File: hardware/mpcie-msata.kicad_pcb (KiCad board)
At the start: 4 copper layers, 100 x 85 mm, 153 parts, among them J101 USB-A, J102 TNG-Power-BTM, J103 TNG-Power-TOP, J104 TNG-Data-BTM, J105 TNG-Data-TOP, P101 Debug, P102 PE, P202 PWR IN, SW101 BOOT, T201 744272251, U101 USB2517, U102 MIC2026-1YM, U103 82400152, U104 STM32F070CBT6, U105 TPD4S010DQA, U106 TPD4S010DQA, U107 TPD4S010DQA, U110 TPS22975, U112 VN7140AS, U201 AZ1117EH, U203 BD90640HFP, U204 PAC1933, X101 24MHz, X102 TBD

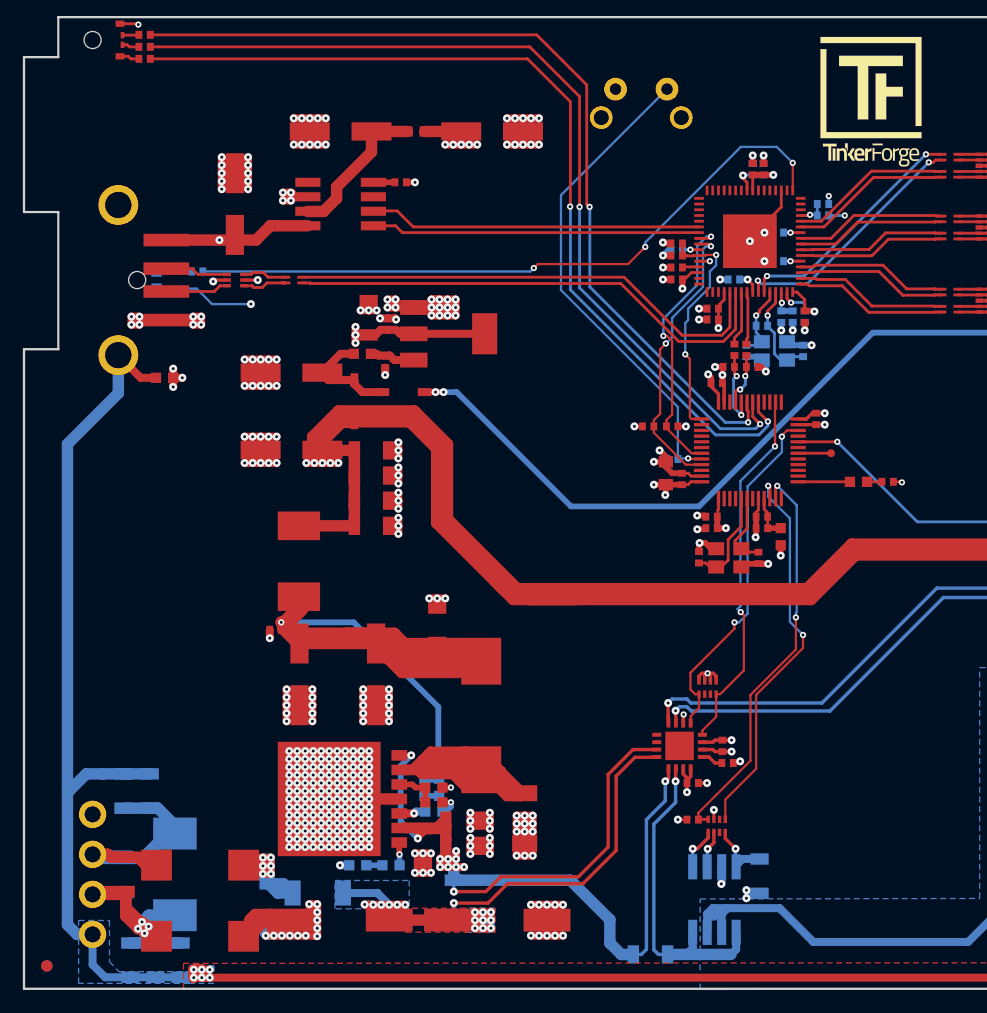
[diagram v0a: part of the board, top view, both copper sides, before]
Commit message: schematic improved
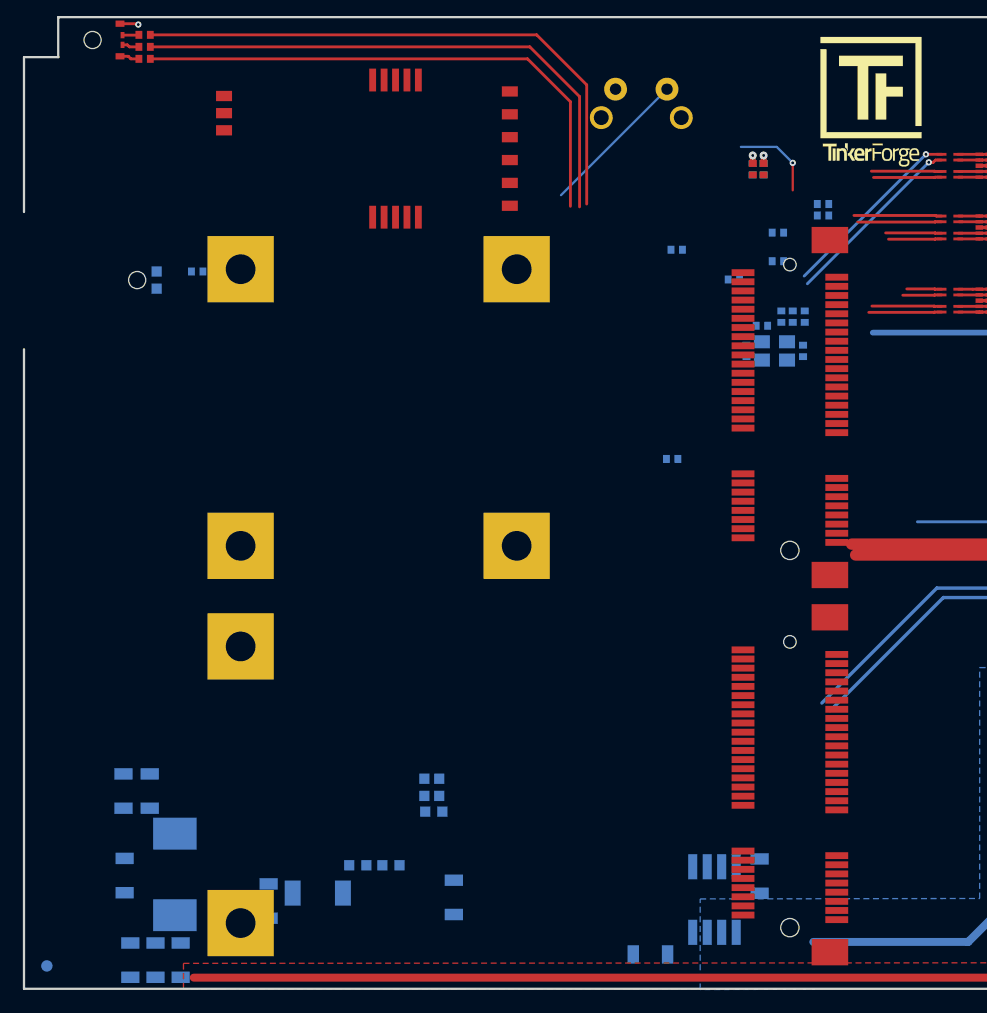
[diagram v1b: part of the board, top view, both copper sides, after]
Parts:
- removed C107, C110, C112, C116, C127, C129, C130, C131, C133, C214, C221, C222: 100nF, C0402F
- removed C108, C109, C117: >100uF, ELKO_63
- removed C115, C123, C124, C209, C226: 1uF, C0402F
- removed C120: 100nF, C0603F
- removed C121, C122: TBD/47pF, C0402F
- removed C137, C138: TBD, C0402F
- removed C139: 10uF, C0805
- removed C201, C202, C215, C218, C223, C224, C225, C227: 10uF, C1206
- removed C203: TBD, kicad-libraries:ELKO_63
- removed C205: 100nF, C1206
- removed C208: 100pF, C0603F
- removed C212, C213: UWT1H221MNL1GS, kicad-libraries:ELKO_103
- removed C216, C219, C220: >100µF, kicad-libraries:ELKO_63
- removed D102: LED, D0603F
- removed D202, D203: B0520LW-7-F, kicad-libraries:SOD-123
- removed D206: PMEG6045, SOD-128
- removed the Fiducial_Mark at (59.5, 133.9)
- removed J101: USB-A, kicad-libraries:USB-A-SMT-8231
- removed L101, L201: INDUCTs, R0603F
- removed L102: 744230900, WE-CNSW-0603
- removed L108: FB, R0603F
- removed L202: 22uH 74437368220, WE-LHMI
- removed L203: 10uH, SRP7030
- removed P101: Debug, kicad-libraries:DEBUG_PAD
- removed P202: PWR IN, OQ_4P
- removed R101, R105, R106, R111, R117, R218: 10k, R0402F
- removed R102: 100k, R0402F
- removed R112, R113: 22, R0402F
- removed R121: 1k, R0402F
- removed R204: VC1206K201R030, R1206
- removed R208: 27, R0603F
- removed RP102, RP201: 10k, kicad-libraries:4X0402
- removed T201: 744272251, kicad-libraries:WE-SL5
- removed U101: USB2517, kicad-libraries:QFN64-9x9mm-0.5mm_USB2517
- removed U102: MIC2026-1YM, kicad-libraries:SO-8
- removed U103: 82400152, SOT563-SPEC
- removed U104: STM32F070CBT6, kicad-libraries:LQFP48
- removed U201: AZ1117EH, kicad-libraries:SOT-223
- removed U203: BD90640HFP, BD906XX-C-HRP7
- removed U204: PAC1933, kicad-libraries:QFN-16
- removed X102: TBD, kicad-libraries:CRYSTAL_3225
- added REF**: Mini-SATA, kicad-libraries:Mini-SATA, F.Cu at (124.5, 122.0)
- added REF**: Mini-PCIE, kicad-libraries:Mini-PCIE, F.Cu at (124.5, 89.0)
- added REF**: LM813, kicad-libraries:LM813, F.Cu at (87.5, 62.5)
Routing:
- net GND: track 859.2 -> 125.7 mm, vias 402 -> 49
- net +5V: track 270.4 -> 115.9 mm, vias 10 -> 0
- net CUR1-: track 104.3 -> 0.00 mm, vias 12 -> 0
- net Net-(C214-Pad1): track 88.7 -> 0.00 mm, vias 1 -> 0
- net Earth: track 251.7 -> 170.1 mm, vias 31 -> 25
- net 3V3: track 78.9 -> 2.33 mm, vias 32 -> 2
- net Net-(R104-Pad1): track 59.3 -> 0.00 mm, vias 3 -> 0
- net Net-(D206-Pad2): track 58.3 -> 0.00 mm
- net CUR1+: track 70.1 -> 12.8 mm, vias 16 -> 0
- net 5V_STACK_UP: track 111.9 -> 60.0 mm, vias 2 -> 0
- net EXT_USB_D+: track 43.8 -> 0.00 mm
- net EXT_USB_D-: track 42.9 -> 0.00 mm
- net Net-(C204-Pad2): track 41.6 -> 0.00 mm, vias 4 -> 0
- net SW_24_STACK: track 35.5 -> 0.00 mm, vias 2 -> 0
- net SW_24_CUR: track 34.5 -> 0.00 mm, vias 2 -> 0
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- removed copper zone on B.Cu, net CUR1+
- removed copper zone on F.Cu, net CUR1+
- removed copper zone on B.Cu, net Earth
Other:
- outline, holes or cut-outs redrawn
- board text removed: "FE"
- board text removed: "GND"
- board text removed: "NC"
- board text removed: "VCC"

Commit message: schematic nearly finished
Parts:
- added REF**: QFP-64_7x7_Pitch0.4mm, kicad-libraries:QFP-64_7x7_Pitch0.4mm, F.Cu at (94.3, 112.2)
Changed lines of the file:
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@@
     (tracks 533)
     (zones 0)
-    (modules 77)
+    (modules 78)
     (nets 66)
   )
@@
     (add_net STACK_USB_D4_F-)
   )
+  (module kicad-libraries:QFP-64_7x7_Pitch0.4mm (layer F.Cu)
+    (at 94.35 112.15)
+    (attr smd)
+    (fp_text reference REF** (at 0 -0.6) (layer F.Fab)
+      (effects (font (size 0.15 0.15) (thickness 0.0375)))
+    )
+    (fp_text value QFP-64_7x7_Pitch0.4mm (at 0 0.6) (layer F.Fab)
+      (effects (font (size 0.15 0.15) (thickness 0.0375)))
+    )
+    (fp_line (start 3.5 -3.5) (end -2.5 -3.5) (layer F.Fab) (width 0.1))
+    (fp_line (start 3.5 3.5) (end 3.5 -3.5) (layer F.Fab) (width 0.1))
+    (fp_line (start -3.5 3.5) (end 3.5 3.5) (layer F.Fab) (width 0.1))
+    (fp_line (start -3.5 -2.5) (end -3.5 3.5) (layer F.Fab) (width 0.1))
+    (fp_line (start -2.5 -3.5) (end -3.5 -2.5) (layer F.Fab) (width 0.1))
+    (pad EP smd rect (at 0 0) (size 4 4) (layers F.Cu F.Paste F.Mask))
+    (pad 64 smd oval (at -3 -4) (size 0.19 1.2) (layers F.Cu F.Paste F.Mask))
+    (pad 63 smd oval (at -2.6 -4) (size 0.19 1.2) (layers F.Cu F.Paste F.Mask))
+    (pad 62 smd oval (at -2.2 -4) (size 0.19 1.2) (layers F.Cu F.Paste F.Mask))
+    (pad 61 smd oval (at -1.8 -4) (size 0.19 1.2) (layers F.Cu F.Paste F.Mask))
+    (pad 60 smd oval (at -1.4 -4) (size 0.19 1.2) (layers F.Cu F.Paste F.Mask))
+    (pad 59 smd oval (at -1 -4) (size 0.19 1.2) (layers F.Cu F.Paste F.Mask))
+    (pad 58 smd oval (at -0.6 -4) (size 0.19 1.2) (layers F.Cu F.Paste F.Mask))
+    (pad 57 smd oval (at -0.2 -4) (size 0.19 1.2) (layers F.Cu F.Paste F.Mask))
+    (pad 56 smd oval (at 0.2 -4) (size 0.19 1.2) (layers F.Cu F.Paste F.Mask))
+    (pad 55 smd oval (at 0.6 -4) (size 0.19 1.2) (layers F.Cu F.Paste F.Mask))
+    (pad 54 smd oval (at 1 -4) (size 0.19 1.2) (layers F.Cu F.Paste F.Mask))
+    (pad 53 smd oval (at 1.4 -4) (size 0.19 1.2) (layers F.Cu F.Paste F.Mask))
+    (pad 52 smd oval (at 1.8 -4) (size 0.19 1.2) (layers F.Cu F.Paste F.Mask))
+    (pad 51 smd oval (at 2.2 -4) (size 0.19 1.2) (layers F.Cu F.Paste F.Mask))
+    (pad 50 smd oval (at 2.6 -4) (size 0.19 1.2) (layers F.Cu F.Paste F.Mask))
+    (pad 49 smd oval (at 3 -4) (size 0.19 1.2) (layers F.Cu F.Paste F.Mask))
+    (pad 48 smd oval (at 4 -3 90) (size 0.19 1.2) (layers F.Cu F.Paste F.Mask))
+    (pad 47 smd oval (at 4 -2.6 90) (size 0.19 1.2) (layers F.Cu F.Paste F.Mask))
+    (pad 46 smd oval (at 4 -2.2 90) (size 0.19 1.2) (layers F.Cu F.Paste F.Mask))
+    (pad 45 smd oval (at 4 -1.8 90) (size 0.19 1.2) (layers F.Cu F.Paste F.Mask))
+    (pad 44 smd oval (at 4 -1.4 90) (size 0.19 1.2) (layers F.Cu F.Paste F.Mask))
+    (pad 43 smd oval (at 4 -1 90) (size 0.19 1.2) (layers F.Cu F.Paste F.Mask))
+    (pad 42 smd oval (at 4 -0.6 90) (size 0.19 1.2) (layers F.Cu F.Paste F.Mask))
+    (pad 41 smd oval (at 4 -0.2 90) (size 0.19 1.2) (layers F.Cu F.Paste F.Mask))
+    (pad 40 smd oval (at 4 0.2 90) (size 0.19 1.2) (layers F.Cu F.Paste F.Mask))
+    (pad 39 smd oval (at 4 0.6 90) (size 0.19 1.2) (layers F.Cu F.Paste F.Mask))
+    (pad 38 smd oval (at 4 1 90) (size 0.19 1.2) (layers F.Cu F.Paste F.Mask))
+    (pad 37 smd oval (at 4 1.4 90) (size 0.19 1.2) (layers F.Cu F.Paste F.Mask))
+    (pad 36 smd oval (at 4 1.8 90) (size 0.19 1.2) (layers F.Cu F.Paste F.Mask))
+    (pad 35 smd oval (at 4 2.2 90) (size 0.19 1.2) (layers F.Cu F.Paste F.Mask))
+    (pad 34 smd oval (at 4 2.6 90) (size 0.19 1.2) (layers F.Cu F.Paste F.Mask))
+    (pad 33 smd oval (at 4 3 90) (size 0.19 1.2) (layers F.Cu F.Paste F.Mask))
+    (pad 32 smd oval (at 3 4) (size 0.19 1.2) (layers F.Cu F.Paste F.Mask))
+    (pad 31 smd oval (at 2.6 4) (size 0.19 1.2) (layers F.Cu F.Paste F.Mask))
+    (pad 30 smd oval (at 2.2 4) (size 0.19 1.2) (layers F.Cu F.Paste F.Mask))
+    (pad 29 smd oval (at 1.8 4) (size 0.19 1.2) (layers F.Cu F.Paste F.Mask))
+    (pad 28 smd oval (at 1.4 4) (size 0.19 1.2) (layers F.Cu F.Paste F.Mask))
+    (pad 27 smd oval (at 1 4) (size 0.19 1.2) (layers F.Cu F.Paste F.Mask))
+    (pad 26 smd oval (at 0.6 4) (size 0.19 1.2) (layers F.Cu F.Paste F.Mask))
+    (pad 25 smd oval (at 0.2 4) (size 0.19 1.2) (layers F.Cu F.Paste F.Mask))
+    (pad 24 smd oval (at -0.2 4) (size 0.19 1.2) (layers F.Cu F.Paste F.Mask))
+    (pad 23 smd oval (at -0.6 4) (size 0.19 1.2) (layers F.Cu F.Paste F.Mask))
+    (pad 22 smd oval (at -1 4) (size 0.19 1.2) (layers F.Cu F.Paste F.Mask))
+    (pad 21 smd oval (at -1.4 4) (size 0.19 1.2) (layers F.Cu F.Paste F.Mask))
+    (pad 20 smd oval (at -1.8 4) (size 0.19 1.2) (layers F.Cu F.Paste F.Mask))
+    (pad 19 smd oval (at -2.2 4) (size 0.19 1.2) (layers F.Cu F.Paste F.Mask))
+    (pad 18 smd oval (at -2.6 4) (size 0.19 1.2) (layers F.Cu F.Paste F.Mask))
+    (pad 17 smd oval (at -3 4) (size 0.19 1.2) (layers F.Cu F.Paste F.Mask))
+    (pad 16 smd oval (at -4 3 90) (size 0.19 1.2) (layers F.Cu F.Paste F.Mask))
+    (pad 15 smd oval (at -4 2.6 90) (size 0.19 1.2) (layers F.Cu F.Paste F.Mask))
+    (pad 14 smd oval (at -4 2.2 90) (size 0.19 1.2) (layers F.Cu F.Paste F.Mask))
+    (pad 13 smd oval (at -4 1.8 90) (size 0.19 1.2) (layers F.Cu F.Paste F.Mask))
+    (pad 12 smd oval (at -4 1.4 90) (size 0.19 1.2) (layers F.Cu F.Paste F.Mask))
+    (pad 11 smd oval (at -4 1 90) (size 0.19 1.2) (layers F.Cu F.Paste F.Mask))
+    (pad 10 smd oval (at -4 0.6 90) (size 0.19 1.2) (layers F.Cu F.Paste F.Mask))
+    (pad 9 smd oval (at -4 0.2 90) (size 0.19 1.2) (layers F.Cu F.Paste F.Mask))
+    (pad 8 smd oval (at -4 -0.2 90) (size 0.19 1.2) (layers F.Cu F.Paste F.Mask))
+    (pad 7 smd oval (at -4 -0.6 90) (size 0.19 1.2) (layers F.Cu F.Paste F.Mask))
+    (pad 6 smd oval (at -4 -1 90) (size 0.19 1.2) (layers F.Cu F.Paste F.Mask))
+    (pad 5 smd oval (at -4 -1.4 90) (size 0.19 1.2) (layers F.Cu F.Paste F.Mask))
+    (pad 4 smd oval (at -4 -1.8 90) (size 0.19 1.2) (layers F.Cu F.Paste F.Mask))
+    (pad 3 smd oval (at -4 -2.2 90) (size 0.19 1.2) (layers F.Cu F.Paste F.Mask))
+    (pad 2 smd oval (at -4 -2.6 90) (size 0.19 1.2) (layers F.Cu F.Paste F.Mask))
+    (pad 1 smd oval (at -4 -3 90) (size 0.19 1.2) (layers F.Cu F.Paste F.Mask))
+  )
   (module kicad-libraries:Mini-SATA (layer F.Cu)

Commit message: fix schematic first placement
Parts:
- removed C210: 4.7nF, C0603F
- removed C211: 10nF, C1206
- removed C217: DNP, C0603F
- removed D101: LED green, LED-LP
- removed D201: 3.0SMI30CATR, kicad-libraries:SMC
- removed D205: PMEG6045, SOD-128
- removed R209: 1M, R1206
- removed R212: 20k, R0603F
- removed R214: 47k, R0603F
- removed R215: 8.2k, R0603F
- removed R219, R220, R221: 0.02, R1206
- removed REF**: QFP-64_7x7_Pitch0.4mm, kicad-libraries:QFP-64_7x7_Pitch0.4mm
- removed REF**: Mini-SATA, kicad-libraries:Mini-SATA
- removed REF**: Mini-PCIE, kicad-libraries:Mini-PCIE
- removed REF**: LM813, kicad-libraries:LM813
- removed U106, U107: TPD4S010DQA, TPD4S010DQA
- removed U110: TPS22975, WSON8-2x2
- removed U112: VN7140AS, kicad-libraries:SO-8
- added C107: 100nF, C0402F, B.Cu at (133.2, 70.2)
- added C108: 1uF, C0402F, F.Cu at (134.1, 67.2)
- added C109: 1uF, C0402F, F.Cu at (132.2, 64.5)
- added C110: 100nF, C0402F, B.Cu at (128.8, 67.2)
- added C112: 100nF, C0402F, B.Cu at (137.8, 63.5)
- added C115: 1uF, C0402F, F.Cu at (133.2, 70.2)
- added C116: 10uF, C0805, F.Cu at (129.3, 59.2)
- added C117: 100nF, C0402F, B.Cu at (134.6, 60.1)
- added C120: 1uF, C0402F, F.Cu at (137.2, 68.0)
- added C121: TBD/47pF, C0402F, F.Cu at (128.0, 71.3)
- added C122: TBD/47pF, C0402F, F.Cu at (128.0, 69.2)
- added C123: 1uF, C0402F, F.Cu at (223.2, 70.8)
- added C124: 1uF, C0402F, F.Cu at (237.8, 87.3)
- added C127: 100nF, C0402F, F.Cu at (230.7, 95.3)
- added C129: 100nF, C0402F, F.Cu at (217.2, 74.2)
- added C130: 100nF, C0402F, F.Cu at (232.1, 87.7)
- added C131: 100nF, C0402F, F.Cu at (224.2, 79.0)
- added C133: 100nF, C0402F, F.Cu at (233.5, 93.4)
- added C137: TBD, C0402F, F.Cu at (222.2, 93.5)
- added C138: TBD, C0402F, F.Cu at (219.3, 70.5)
- added C139: 10uF, C0805, F.Cu at (201.1, 96.1)
- added C140: 10uF, C0805, F.Cu at (139.4, 94.0)
- added C141: 1uF, C0402F, F.Cu at (126.5, 57.8)
- added C142: 1uF, C0402F, F.Cu at (140.8, 94.5)
- added C143: 1uF, C0402F, F.Cu at (146.9, 92.7)
- added C144: 1uF, C0402F, F.Cu at (134.4, 53.4)
- added C145: >100uF, ELKO_63, F.Cu at (103.0, 61.8)
- added C146: 10uF, C0805, F.Cu at (146.7, 91.3)
- added C147: 10uF, C0805, F.Cu at (135.8, 53.9)
- added C148: >100uF, ELKO_63, F.Cu at (144.8, 87.2)
- added C150: >100uF, ELKO_63, F.Cu at (139.9, 57.2)
- added C151: >100uF, ELKO_63, F.Cu at (153.7, 87.2)
- added C201: 10uF, C0805, B.Cu at (115.0, 128.1)
- added C202: >100uF, ELKO_63, F.Cu at (129.4, 107.5)
- added C203: 10uF, C0805, B.Cu at (115.0, 116.0)
- added C205: 10uF, C0805, B.Cu at (124.0, 108.5)
- added C208: 10uF, C0805, B.Cu at (100.8, 60.0)
- added C209: 10uF, C0805, F.Cu at (135.8, 102.2)
- added C301: 10uF, C0805, B.Cu at (115.0, 95.0)
- added C302: 10uF, C0805, B.Cu at (115.0, 83.2)
- added C303: 10uF, C0805, B.Cu at (124.0, 78.8)
- added C304: 10uF, C0805, B.Cu at (124.0, 75.5)
- added C305: 10uF, C0805, B.Cu at (115.0, 72.7)
- added C306: >100uF, ELKO_63, F.Cu at (129.6, 93.8)
- added C308: 100nF, kicad-libraries:C0402E, F.Cu at (359.6, 80.7)
- added C309: 10uF, C0805, F.Cu at (135.8, 93.8)
- added C310: 10nF, kicad-libraries:C0402E, F.Cu at (126.2, 79.8)
- added C311: 10nF, kicad-libraries:C0402E, F.Cu at (126.2, 81.0)
- added C312: 10nF, kicad-libraries:C0402E, F.Cu at (126.2, 83.0)
- added C313: 10nF, kicad-libraries:C0402E, F.Cu at (126.2, 84.2)
- added C314: 100nF, kicad-libraries:C0402E, F.Cu at (343.2, 95.2)
- added C315: 100nF, kicad-libraries:C0402E, F.Cu at (346.3, 92.4)
- added C316: 100nF, kicad-libraries:C0402E, F.Cu at (334.6, 104.0)
- added C317: 100nF, kicad-libraries:C0402E, F.Cu at (338.9, 97.6)
- added C318: 100nF, kicad-libraries:C0402E, F.Cu at (356.6, 80.7)
- added C319: 100nF, kicad-libraries:C0402E, F.Cu at (334.6, 100.2)
- added C320: 100nF, kicad-libraries:C0402E, F.Cu at (347.6, 89.6)
- added C321: 100nF, kicad-libraries:C0402E, F.Cu at (334.6, 102.1)
- added C322: 100nF, kicad-libraries:C0402E, F.Cu at (350.6, 89.6)
- added C323: 100nF, kicad-libraries:C0402E, F.Cu at (356.6, 82.6)
- added C324: 100nF, kicad-libraries:C0402E, F.Cu at (349.3, 91.5)
- added C325: 10uF, C0805, F.Cu at (348.2, 84.7)
- added C326: 10uF, C0805, F.Cu at (335.3, 98.0)
- added C327: 10uF, C0805, F.Cu at (353.0, 81.0)
- added C328: 10uF, C0805, F.Cu at (343.9, 90.2)
- added C329: 10uF, C0805, F.Cu at (366.6, 68.3)
- added C330: 10uF, C0805, F.Cu at (343.9, 87.6)
- added C331: 10uF, C0805, F.Cu at (353.0, 78.4)
- added C332: 100nF, kicad-libraries:C0402E, F.Cu at (354.9, 86.4)
- added C333: 100nF, kicad-libraries:C0402E, F.Cu at (337.6, 102.1)
- added C334: 100nF, kicad-libraries:C0402E, F.Cu at (337.6, 104.0)
- added C335: 100nF, kicad-libraries:C0402E, F.Cu at (340.6, 99.5)
- added C336: 100nF, kicad-libraries:C0402E, F.Cu at (346.3, 94.3)
- added C337: 100nF, kicad-libraries:C0402E, F.Cu at (354.9, 84.5)
- added C338: 100nF, kicad-libraries:C0402E, F.Cu at (373.2, 67.9)
- added C339: 10uF, C0805, F.Cu at (335.3, 90.2)
- added C340: 10uF, C0805, F.Cu at (339.6, 87.6)
- added C341: 10uF, C0805, F.Cu at (335.3, 87.6)
- added C342: 10uF, C0805, F.Cu at (339.6, 85.0)
- added C343: 100nF, kicad-libraries:C0402E, F.Cu at (351.9, 87.2)
- added C344: 100nF, kicad-libraries:C0402E, F.Cu at (370.2, 69.8)
- added C345: 10uF, C0805, F.Cu at (339.9, 79.8)
- added C346: 10uF, C0805, F.Cu at (335.3, 95.4)
- added C347: 100nF, kicad-libraries:C0402E, F.Cu at (337.6, 100.2)
- added D102: LED, D0603F, F.Cu at (117.2, 57.6)
- added J201: Mini-PCIE, kicad-libraries:Mini-PCIE, F.Cu at (119.5, 121.0)
- added J202: SIM8060, kicad-libraries:SIM8060, F.Cu at (133.2, 115.0)
- added J301: Mini-SATA, kicad-libraries:Mini-SATA, F.Cu at (119.5, 88.0)
- added L101: FB, R0603F, F.Cu at (131.2, 60.6)
- added L102: 744230900, WE-CNSW-0603, B.Cu at (128.3, 74.5)
- added L108: FB, R0603F, F.Cu at (225.0, 86.6)
- added L111: INDUCTs, kicad-libraries:R0805E, B.Cu at (150.2, 85.3)
- added L112: INDUCTs, kicad-libraries:R0805E, F.Cu at (146.7, 54.5)
- added L201: INDUCTs, kicad-libraries:R0805E, F.Cu at (134.8, 104.8)
- added L301: INDUCTs, kicad-libraries:R0805E, F.Cu at (134.8, 96.5)
- added L302: INDUCTs, kicad-libraries:R0805E, F.Cu at (353.0, 75.8)
- added L303: INDUCTs, kicad-libraries:R0805E, F.Cu at (339.6, 90.2)
- added L304: INDUCTs, kicad-libraries:R0805E, F.Cu at (335.3, 92.8)
- added L305: INDUCTs, kicad-libraries:R0805E, F.Cu at (343.9, 85.0)
- added P101: Debug, kicad-libraries:DEBUG_PAD, F.Cu at (218.2, 65.2)
- added Q301: 40MHz, kicad-libraries:CRYSTAL_3225, F.Cu at (335.4, 80.3)
- added R101: 10k, R0402F, B.Cu at (137.8, 62.5)
- added R102: 10k, R0402F, F.Cu at (128.2, 65.8)
- added R105: 10k, R0402F, B.Cu at (129.3, 61.2)
- added R106: 10k, R0402F, F.Cu at (235.0, 89.6)
- added R111: DNP, R0402F, F.Cu at (232.1, 91.5)
- added R112: 22, R0402F, B.Cu at (128.3, 69.8)
- added R113: 22, R0402F, B.Cu at (128.3, 70.8)
- added R117: 10k, R0402F, F.Cu at (211.6, 82.8)
- added R121: 1k, R0402F, F.Cu at (117.2, 55.1)
- added R122: 100k, R0402F, B.Cu at (136.2, 58.8)
- added R123: 169k, R0402F, B.Cu at (140.2, 96.3)
- added R124: 30.1k, R0402F, B.Cu at (142.2, 96.3)
- added R201: 1k, kicad-libraries:R0402F, B.Cu at (120.8, 118.5)
- added R202: 1k, kicad-libraries:R0402F, F.Cu at (112.2, 118.2)
- added R203: 1k, kicad-libraries:R0402F, F.Cu at (112.2, 117.2)
- added R204: DNP, kicad-libraries:R0402F, B.Cu at (133.8, 116.8)
- added R205: 1k, kicad-libraries:R0402F, B.Cu at (90.5, 58.8)
- added R301: 0, kicad-libraries:R0402F, F.Cu at (334.6, 107.8)
- added R302: DNP, kicad-libraries:R0402F, F.Cu at (373.2, 69.8)
- added R303: DNP, kicad-libraries:R0402F, F.Cu at (346.2, 96.2)
- added R304: DNP, kicad-libraries:R0402F, F.Cu at (343.6, 99.0)
- added R305: DNP, kicad-libraries:R0402F, F.Cu at (337.6, 105.9)
- added R306: 10k, kicad-libraries:R0402F, F.Cu at (354.8, 88.3)
- added R307: 10k, kicad-libraries:R0402F, F.Cu at (349.3, 93.4)
- added R308: 10k, kicad-libraries:R0402F, F.Cu at (365.0, 78.5)
- added R309: DNP, kicad-libraries:R0402F, F.Cu at (368.9, 74.7)
- added R310: DNP, kicad-libraries:R0402F, F.Cu at (365.0, 76.6)
- added R311: 10k, kicad-libraries:R0402F, F.Cu at (370.0, 71.7)
- added R312: 10k, kicad-libraries:R0402F, F.Cu at (357.9, 84.5)
- added R313: 10k, kicad-libraries:R0402F, F.Cu at (340.6, 101.4)
- added RP201: 1k, kicad-libraries:4X0402, B.Cu at (111.7, 106.5)
- added RP202: 1k, kicad-libraries:4X0402, B.Cu at (101.2, 69.5)
- added RP301: 1k, kicad-libraries:4X0402, F.Cu at (351.9, 84.8)
- added RP302: 100, kicad-libraries:4X0402, F.Cu at (141.6, 82.5)
- added U101: USB2514B, kicad-libraries:QFN36-6x6mm-0.5mm, B.Cu at (133.2, 65.3)
- added U102: LD1117, kicad-libraries:SOT-223, F.Cu at (129.4, 55.1)
- added U103: TPS7A7002, kicad-libraries:SO-8-EP, F.Cu at (145.3, 95.8)
- added U104: STM32F070CBT6, kicad-libraries:LQFP48, B.Cu at (120.0, 65.5)
- added U201: LM813, kicad-libraries:LM813, F.Cu at (86.0, 62.0)
- added U301: TUSB9261PVP, kicad-libraries:QFP-64_7x7_Pitch0.4mm, F.Cu at (134.1, 81.7)
- added U302: TLV71211DBVR, kicad-libraries:SOT23-5, F.Cu at (366.5, 71.6)
- added U303: AP7333-18SAG-7, kicad-libraries:SOT23-3, F.Cu at (361.5, 76.5)
- added U304: AT25DF011-SSHN-T, kicad-libraries:SO-8, B.Cu at (105.7, 81.2)
- added X102: TBD, kicad-libraries:CRYSTAL_3225, F.Cu at (223.9, 61.5)
- C103: value 1uF -> 100nF
- C104, R110, R114: moved to F.Cu
- C105: value 1uF -> 100nF; moved to F.Cu
- C111, C113: value 100nF -> 1uF; moved to F.Cu
- C118: value 100nF -> 1uF
- C125: value 1uF -> 10uF; footprint C0402F -> C0805
- C126: value 1uF -> 1nF; moved to B.Cu
- C128: value 1µF -> 10uF; footprint C0402F -> C0805
- C132: value DNP -> 10uF; footprint C0402F -> C0805
- C135: value 10uF -> 1uF; footprint C1206 -> C0402F
- C136: footprint C1206 -> C0805
- C204: value 10nF -> 10uF; footprint C1206 -> C0805
- C206: value 1nF 2kV -> 10uF; footprint C1206 -> C0805
- C207: value 1nF 2kV -> 10uF; footprint C1206 -> C0805; moved to F.Cu
- L103: value 744230900 -> FB; footprint WE-CNSW-0603 -> R0603F
- L104, R116: moved to B.Cu
- L106, L107, L110: value 744230900 -> INDUCTs; footprint WE-CNSW-0603 -> kicad-libraries:R0805E
- L109: value 742792040 -> 744230900; footprint kicad-libraries:R0805 -> kicad-libraries:WE-CNSW-0603
- R104: value 1k -> 10k; moved to F.Cu
- R107: value 10k -> DNP; moved to F.Cu
- R109: value DNP -> 10k; moved to F.Cu
- R118: value 1k -> DNP; footprint kicad-libraries:1206 -> R0402F
- R206, R207: value VC1206K201R030 -> 1k; footprint R1206 -> kicad-libraries:R0402F
- U105: value TPD4S010DQA -> 82400152; footprint TPD4S010DQA -> SOT563-SPEC
- moved C118 213.5 mm to (327.9, 118.0), turned to 0 degrees
- moved R114 104.5 mm to (212.5, 54.2)
- moved G*** 97.5 mm to (62.9, 127.3)
- moved R207 77.8 mm to (88.5, 58.8), turned to 270 degrees
- moved R118 67.5 mm to (136.7, 60.2), turned to 0 degrees
- moved C207 64.9 mm to (130.7, 113.3), turned to 0 degrees
- moved C204 59.4 mm to (124.0, 111.8), turned to 90 degrees
- moved R104 56.4 mm to (128.2, 63.9)
- moved R206 52.1 mm to (88.5, 70.5), turned to 270 degrees
- moved C206 50.5 mm to (115.0, 105.8)
- moved C128 39.0 mm to (127.8, 61.6), turned to 90 degrees
- moved R116 39.0 mm to (134.6, 59.0)
- moved C136 35.3 mm to (126.0, 59.2), turned to 0 degrees
- moved C126 33.5 mm to (136.7, 61.2), turned to 0 degrees
- moved L109 30.8 mm to (138.4, 64.8), turned to 0 degrees
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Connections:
- C104 pad 1: Net-(C103-Pad1) -> Net-(C104-Pad1)
- C106 pad 1: Net-(C105-Pad1) -> Net-(C103-Pad1)
- C111 pad 1: 3V3 -> Net-(C103-Pad1)
- C113 pad 1: 3V3 -> Net-(C103-Pad1)
- C114 pad 1: 3V3 -> Net-(C107-Pad1)
- C118 pad 1: 3V3 -> Net-(C107-Pad1)
- C119 pad 1: 3V3 -> Net-(C107-Pad1)
- C125 pad 1: GND -> 3V3
- C125 pad 2: +5V -> GND
- C126 pad 1: GND -> Net-(C126-Pad1)
- C126 pad 2: Net-(C126-Pad2) -> GND
- C128 pad 1: Net-(C126-Pad2) -> 3V3
- C132 pad 1: Net-(C132-Pad1) -> +3.3VP
- C134 pad 1: GND -> 3V3
- C134 pad 2: CUR3- -> GND
- C135 pad 1: GND -> +3.3VP
- C135 pad 2: CUR3- -> GND
- C136 pad 1: GND -> Net-(C136-Pad1)
- C136 pad 2: CUR3- -> GND
- C204 pad 1: Net-(C204-Pad1) -> GND
- C204 pad 2: Net-(C204-Pad2) -> Net-(C201-Pad1)
- C206 pad 1: Net-(C204-Pad1) -> GND
- C206 pad 2: Earth -> Net-(C201-Pad1)
- C207 pad 1: Earth -> Net-(C207-Pad1)
- C207 pad 2: Net-(C204-Pad2) -> GND
- J102 pad 1: GND -> PWR-GND
- J102 pad 10: Net-(J102-Pad10) -> PWR-VCC
- J102 pad 11: GND -> PWR-GND
- J102 pad 12: Net-(J102-Pad10) -> PWR-VCC
- J102 pad 13: GND -> PWR-GND
- J102 pad 14: Net-(J102-Pad10) -> PWR-VCC
- J102 pad 15: GND -> PWR-GND
- J102 pad 16: Net-(J102-Pad10) -> PWR-VCC
- J102 pad 17: GND -> PWR-GND
- J102 pad 18: Net-(J102-Pad10) -> PWR-VCC
- J102 pad 19: GND -> PWR-GND
- J102 pad 2: Net-(J102-Pad10) -> PWR-VCC
- J102 pad 20: Net-(J102-Pad10) -> PWR-VCC
- J102 pad 3: GND -> PWR-GND
- J102 pad 4: Net-(J102-Pad10) -> PWR-VCC
- J102 pad 5: GND -> PWR-GND
- J102 pad 6: Net-(J102-Pad10) -> PWR-VCC
- J102 pad 7: GND -> PWR-GND
- J102 pad 8: Net-(J102-Pad10) -> PWR-VCC
- J102 pad 9: GND -> PWR-GND
- J103 pad 1: STACKPWR -> PWR-VCC
- J103 pad 10: GND -> PWR-GND
- J103 pad 11: STACKPWR -> PWR-VCC
- J103 pad 12: GND -> PWR-GND
- J103 pad 13: STACKPWR -> PWR-VCC
- J103 pad 14: GND -> PWR-GND
- J103 pad 15: STACKPWR -> PWR-VCC
- J103 pad 16: GND -> PWR-GND
- J103 pad 17: STACKPWR -> PWR-VCC
- J103 pad 18: GND -> PWR-GND
- J103 pad 19: STACKPWR -> PWR-VCC
- J103 pad 2: GND -> PWR-GND
- J103 pad 20: GND -> PWR-GND
- J103 pad 3: STACKPWR -> PWR-VCC
- J103 pad 4: GND -> PWR-GND
- J103 pad 5: STACKPWR -> PWR-VCC
- J103 pad 6: GND -> PWR-GND
- J103 pad 7: STACKPWR -> PWR-VCC
- J103 pad 8: GND -> PWR-GND
- J103 pad 9: STACKPWR -> PWR-VCC
- J104 pad 12: (no net) -> Net-(J104-Pad12)
- J104 pad 14: (no net) -> Net-(J104-Pad14)
- J104 pad 15: 5V_STACK_UP -> 5V-STACK
- J104 pad 16: 5V_STACK_UP -> 5V-STACK
- J104 pad 20: (no net) -> Net-(J104-Pad20)
- J104 pad 22: (no net) -> Net-(J104-Pad22)
- J104 pad 23: 5V_STACK_UP -> 5V-STACK
- J104 pad 24: 5V_STACK_UP -> 5V-STACK
- J104 pad 28: (no net) -> Net-(J104-Pad28)
- J104 pad 30: (no net) -> Net-(J104-Pad30)
- J104 pad 31: 5V_STACK_UP -> 5V-STACK
- J104 pad 32: 5V_STACK_UP -> 5V-STACK
- J104 pad 36: (no net) -> Net-(J104-Pad36)
- J104 pad 39: 5V_STACK_UP -> 5V-STACK
- J104 pad 40: 5V_STACK_UP -> 5V-STACK
- J104 pad 7: 5V_STACK_UP -> 5V-STACK
- J104 pad 8: 5V_STACK_UP -> 5V-STACK
- J105 pad 11: STACK_USB_D1_F+ -> Net-(J104-Pad20)
- J105 pad 13: STACK_USB_D1_F- -> Net-(J104-Pad22)
- J105 pad 15: CUR3- -> 5V-STACK
- J105 pad 16: CUR3- -> 5V-STACK
- J105 pad 19: STACK_USB_D2_F+ -> Net-(J104-Pad28)
- J105 pad 21: STACK_USB_D2_F- -> Net-(J104-Pad30)
- J105 pad 23: CUR3- -> 5V-STACK
- J105 pad 24: CUR3- -> 5V-STACK
- J105 pad 27: STACK_USB_D3_F+ -> Net-(J104-Pad36)
- J105 pad 29: STACK_USB_D3_F- -> (no net)
- J105 pad 3: STACK_USB_D0_F+ -> Net-(J104-Pad12)
- J105 pad 31: CUR3- -> 5V-STACK
- J105 pad 32: CUR3- -> 5V-STACK
- J105 pad 35: STACK_USB_D4_F+ -> (no net)
- J105 pad 37: STACK_USB_D4_F- -> (no net)
- J105 pad 39: CUR3- -> 5V-STACK
- J105 pad 40: CUR3- -> 5V-STACK
- J105 pad 5: STACK_USB_D0_F- -> Net-(J104-Pad14)
- J105 pad 7: CUR3- -> 5V-STACK
- J105 pad 8: CUR3- -> 5V-STACK
- L103 pad 1: STACK_USB_D0+ -> 3V3
- L103 pad 2: STACK_USB_D0_F+ -> Net-(C107-Pad1)
- L104 pad 1: STACK_USB_D1+ -> Net-(L104-Pad1)
- L104 pad 2: STACK_USB_D1_F+ -> LM813_DP
- L104 pad 3: STACK_USB_D1_F- -> LM813_DM
- L104 pad 4: STACK_USB_D1- -> Net-(L104-Pad4)
- L105 pad 1: STACK_USB_D2+ -> MSATA_DP
- L105 pad 2: STACK_USB_D2_F+ -> Net-(L105-Pad2)
- L105 pad 3: STACK_USB_D2_F- -> Net-(L105-Pad3)
- L105 pad 4: STACK_USB_D2- -> MSATA_DM
- L106 pad 1: STACK_USB_D3+ -> 3V3
- L106 pad 2: STACK_USB_D3_F+ -> Net-(C136-Pad1)
- L107 pad 1: STACK_USB_D4+ -> +3.3VP
- L107 pad 2: STACK_USB_D4_F+ -> Net-(C140-Pad1)
- L109 pad 1: +5V -> UP_USB_DP
- L109 pad 2: Net-(C126-Pad2) -> Net-(L109-Pad2)
- L110 pad 1: UP_USB_D+ -> 5V-STACK
- L110 pad 2: Net-(J104-Pad4) -> 5V
- R104 pad 2: Net-(D101-Pad2) -> 3V3
- R109 pad 1: Net-(R108-Pad1) -> Net-(R107-Pad1)
- R109 pad 2: GND -> 3V3
- R116 pad 1: SW_5_STACK -> 3V3
- R116 pad 2: 3V3 -> USB_RESET
- R118 pad 1: GND -> Net-(C126-Pad1)
- R118 pad 2: Net-(R118-Pad2) -> GND
- R206 pad 1: Net-(C204-Pad1) -> LM813_WLAN_DIS
- R206 pad 2: Earth -> +3.3VP
- R207 pad 1: Earth -> LM813_EN
- R207 pad 2: Net-(C204-Pad2) -> GND
- U105 pad 1: Net-(J104-Pad4) -> Net-(L109-Pad2)
- U105 pad 2: Net-(J104-Pad6) -> GND
- U105 pad 3: GND -> Net-(L109-Pad3)
- U105 pad 4: STACK_USB_D0_F+ -> Net-(J104-Pad6)
- U105 pad 5: STACK_USB_D0_F- -> 5V-STACK
- U105 pad 6: STACK_USB_D0_F- -> Net-(J104-Pad4)
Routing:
- net +5V: track 115.9 -> 0.00 mm
- net CUR3-: track 98.0 -> 0.00 mm, vias 1 -> 0
- net 5V-STACK: track 0.00 -> 95.8 mm
- net 5V_STACK_UP: track 60.0 -> 0.00 mm
- net STACKPWR: track 56.9 -> 0.00 mm, vias 10 -> 0
- net GND: track 125.7 -> 69.6 mm, vias 49 -> 20
- net CUR3+: track 55.7 -> 0.00 mm, vias 1 -> 0
- net PWR-VCC: track 0.00 -> 49.7 mm, vias 0 -> 10
- net PWR-GND: track 0.00 -> 34.1 mm, vias 0 -> 10
- net Net-(J102-Pad10): track 23.9 -> 0.00 mm
- net LEDB: track 50.4 -> 33.8 mm
- net UP_USB_D+: track 16.4 -> 0.00 mm, vias 1 -> 0
- net UP_USB_D-: track 16.2 -> 0.00 mm, vias 1 -> 0
- net SW_5_STACK: track 16.0 -> 0.00 mm, vias 1 -> 0
- net LEDG: track 49.0 -> 33.2 mm
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- added copper zone on F.Cu, net 5V-STACK
- removed copper zone on VCC, net 3V3
- removed copper zone on F.Cu, net CUR3+
- removed copper zone on F.Cu, net CUR3-
- removed copper zone on GND, net GND
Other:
- outline, holes or cut-outs redrawn
- board text added: "MPCIE-MSATA-WIFI/BT REV 1.0"
- board text removed: "HUB REV 1.0"

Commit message: placement nearly finished
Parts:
- C118, C308, C315, C316, C318, C319, C321, C323, C324, C325, C326, C327, C328, C329, C330, C331, C335, C337, C338, C341, C347, L302, L303, P101, Q301, R114, R301, R302, R303, R304, R305, R308, R310, R311, R312, R313, U302, U303: moved to B.Cu
- U104: moved to F.Cu
- moved R311 263.7 mm to (106.3, 76.0), turned to 270 degrees
- moved R310 261.2 mm to (103.8, 76.0), turned to 90 degrees
- moved R312 252.9 mm to (105.0, 86.3), turned to 90 degrees
- moved C329 248.0 mm to (119.0, 82.2), turned to 270 degrees
- moved C338 242.4 mm to (131.4, 83.8), turned to 180 degrees
- moved R302 242.0 mm to (131.8, 87.7), turned to 270 degrees
- moved U302 240.3 mm to (126.8, 87.2), turned to 180 degrees
- moved U303 240.1 mm to (121.5, 82.3), turned to 180 degrees
- moved R313 239.6 mm to (102.1, 78.3), turned to 180 degrees
- moved C347 235.9 mm to (102.3, 83.3), turned to 270 degrees
- moved C308 232.8 mm to (126.8, 80.5)
- moved C331 232.1 mm to (120.8, 76.7), turned to 90 degrees
- moved R308 229.8 mm to (135.2, 77.1)
- moved C344 229.5 mm to (140.8, 72.9), turned to 90 degrees
- moved R309 226.8 mm to (142.2, 81.0), turned to 180 degrees
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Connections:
- L109 pad 1: UP_USB_DP -> Net-(L109-Pad1)
- L109 pad 2: Net-(L109-Pad2) -> UP_USB_DP
- L109 pad 3: Net-(L109-Pad3) -> UP_USB_DM
- L109 pad 4: UP_USB_DM -> Net-(L109-Pad4)
- U105 pad 1: Net-(L109-Pad2) -> Net-(L109-Pad4)
- U105 pad 3: Net-(L109-Pad3) -> Net-(L109-Pad1)
- U105 pad 4: Net-(J104-Pad6) -> Net-(J104-Pad4)
- U105 pad 6: Net-(J104-Pad4) -> Net-(J104-Pad6)
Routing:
- net MPCIE_DM: track 0.00 -> 48.2 mm, vias 0 -> 1
- net MPCIE_DP: track 0.00 -> 47.8 mm, vias 0 -> 1
- net LM813_DM: track 0.00 -> 35.5 mm, vias 0 -> 1
- net LM813_DP: track 0.00 -> 33.2 mm, vias 0 -> 1
- net GND: track 69.6 -> 93.0 mm, vias 20 -> 36
- net 3V3: track 1.63 -> 19.1 mm, vias 1 -> 13
- net STM_USB_DM: track 0.00 -> 16.9 mm, vias 0 -> 2
- net STM_USB_DP: track 0.00 -> 16.8 mm, vias 0 -> 2
- net Net-(C144-Pad1): track 0.00 -> 13.9 mm
- net Net-(C107-Pad1): track 0.00 -> 12.7 mm, vias 0 -> 4
- net Net-(C136-Pad1): track 0.00 -> 12.5 mm
- net Net-(L102-Pad4): track 0.00 -> 9.47 mm
- net Net-(L102-Pad1): track 0.00 -> 8.84 mm
- net Net-(C101-Pad1): track 0.00 -> 7.83 mm
- net Net-(L104-Pad4): track 0.00 -> 6.59 mm
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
